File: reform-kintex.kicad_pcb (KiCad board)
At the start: 8 copper layers, 60 x 67.8 mm, 38 parts, among them J1 Conn_01x33, U1 MNT Reform 2.0 SoM Socket, U2 XC7K160T-FFG676, U3 MT41K512M16HA-125 :A, U4 MT41K512M16HA-125 :A, U5 TPS51200DRC, U6 KSZ9031RNXCA, U7 TUSB1310ZAY, U8 TC358867XBG, U9 SiI9022A

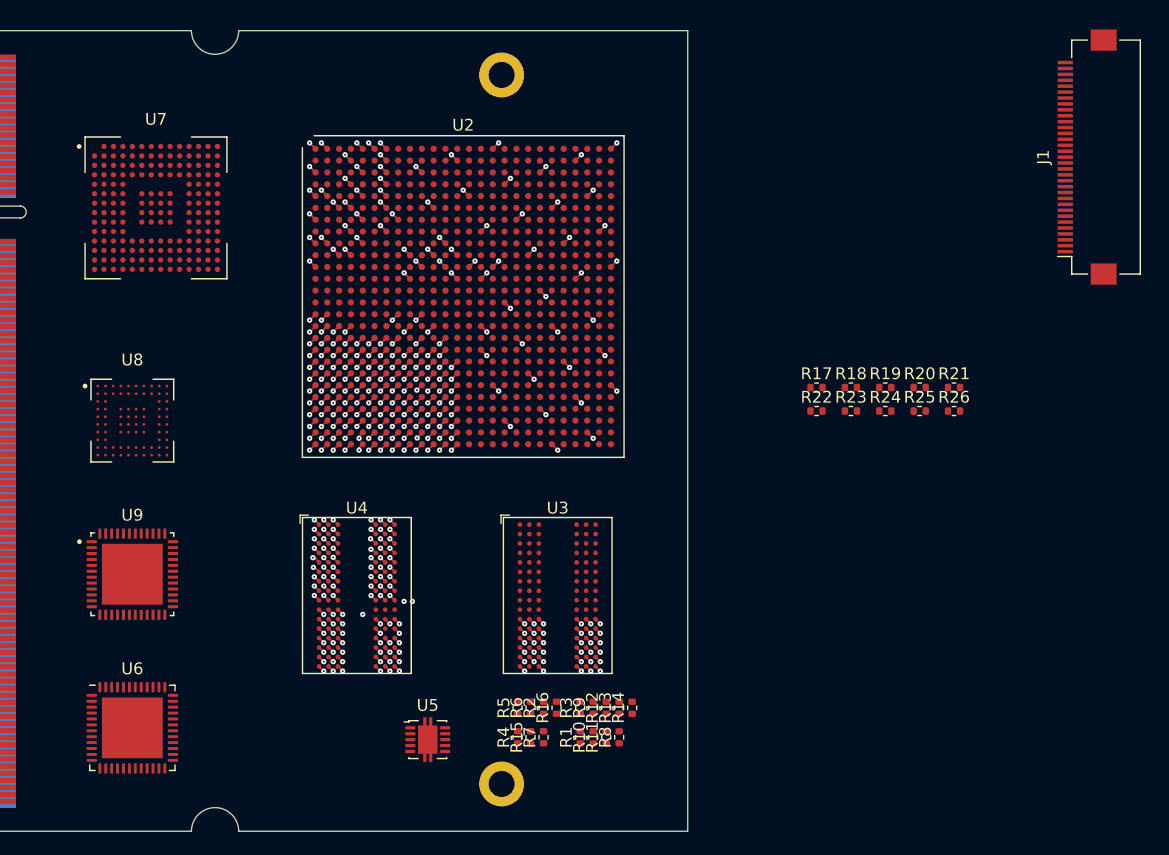
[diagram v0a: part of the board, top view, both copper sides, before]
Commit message: some work on 6 power supplies, SPI flash
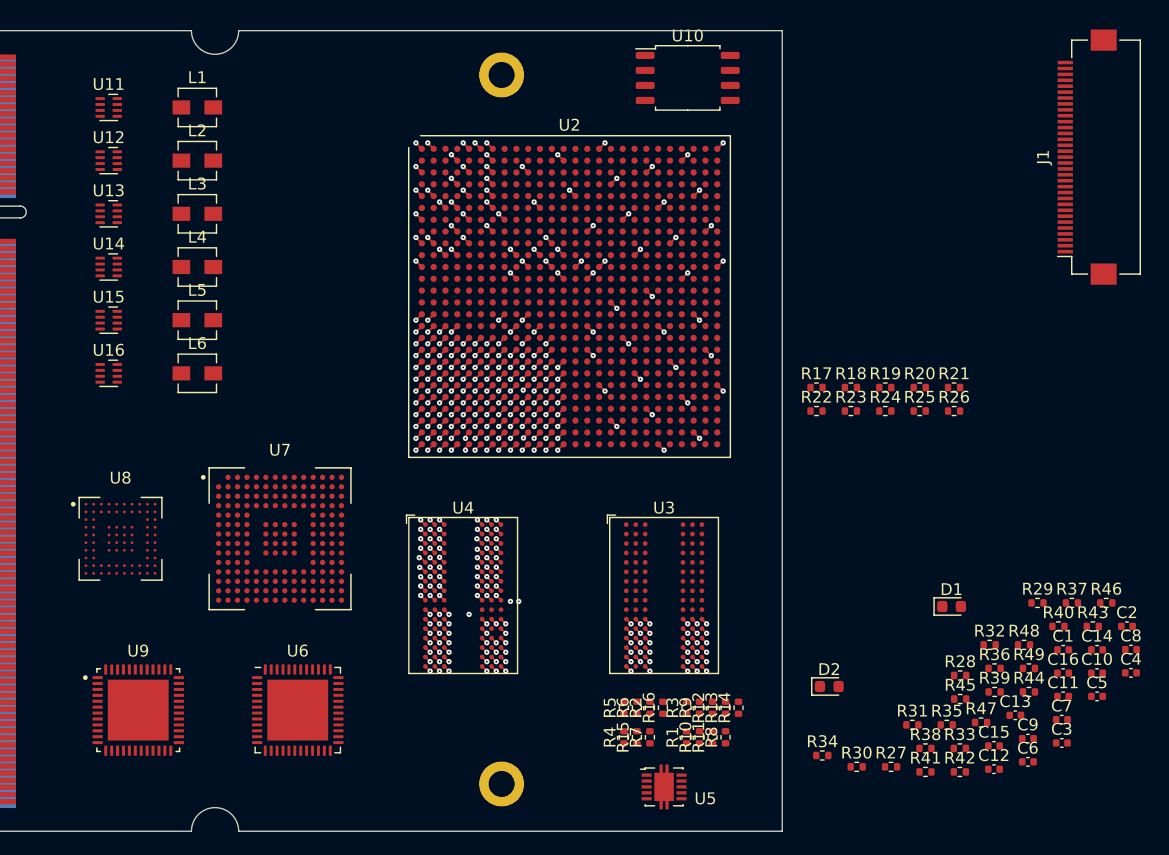
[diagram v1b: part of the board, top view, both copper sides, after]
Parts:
- added C1: 0.1uF, Capacitor_SMD:C_0402_1005Metric, F.Cu at (191.8, 152.4)
- added C10: 0.1uF, Capacitor_SMD:C_0402_1005Metric, F.Cu at (194.6, 154.4)
- added C11: 120p, Capacitor_SMD:C_0402_1005Metric, F.Cu at (191.8, 156.3)
- added C12: 120p, Capacitor_SMD:C_0402_1005Metric, F.Cu at (185.9, 162.5)
- added C13: 120p, Capacitor_SMD:C_0402_1005Metric, F.Cu at (187.7, 157.9)
- added C14: 120p, Capacitor_SMD:C_0402_1005Metric, F.Cu at (194.6, 152.4)
- added C15: 120p, Capacitor_SMD:C_0402_1005Metric, F.Cu at (185.9, 160.5)
- added C16: 120p, Capacitor_SMD:C_0402_1005Metric, F.Cu at (191.8, 154.4)
- added C2: 0.1uF, Capacitor_SMD:C_0402_1005Metric, F.Cu at (197.2, 150.4)
- added C3: 0.1uF, Capacitor_SMD:C_0402_1005Metric, F.Cu at (191.7, 160.3)
- added C4: 0.1uF, Capacitor_SMD:C_0402_1005Metric, F.Cu at (197.5, 154.3)
- added C5: 0.1uF, Capacitor_SMD:C_0402_1005Metric, F.Cu at (194.6, 156.3)
- added C6: 0.1uF, Capacitor_SMD:C_0402_1005Metric, F.Cu at (188.8, 161.9)
- added C7: 0.1uF, Capacitor_SMD:C_0402_1005Metric, F.Cu at (191.7, 158.3)
- added C8: 0.1uF, Capacitor_SMD:C_0402_1005Metric, F.Cu at (197.5, 152.4)
- added C9: 0.1uF, Capacitor_SMD:C_0402_1005Metric, F.Cu at (188.8, 159.9)
- added D1: LED_Small, LED_SMD:LED_0603_1608Metric, F.Cu at (182.3, 148.7)
- added D2: LED_Small, LED_SMD:LED_0603_1608Metric, F.Cu at (172.0, 155.5)
- added L1: IHLP1212AEERR47M11, Inductor_SMD:L_Vishay_IHLP-1212, F.Cu at (118.5, 106.5)
- added L2: IHLP1212AEERR47M11, Inductor_SMD:L_Vishay_IHLP-1212, F.Cu at (118.5, 111.0)
- added L3: IHLP1212AEERR47M11, Inductor_SMD:L_Vishay_IHLP-1212, F.Cu at (118.5, 115.5)
- added L4: IHLP1212AEERR47M11, Inductor_SMD:L_Vishay_IHLP-1212, F.Cu at (118.5, 120.0)
- added L5: IHLP1212AEERR47M11, Inductor_SMD:L_Vishay_IHLP-1212, F.Cu at (118.5, 124.5)
- added L6: IHLP1212AEERR47M11, Inductor_SMD:L_Vishay_IHLP-1212, F.Cu at (118.5, 129.0)
- added R27: 2k2, Resistor_SMD:R_0402_1005Metric, F.Cu at (177.2, 162.3)
- added R28: 0, Resistor_SMD:R_0402_1005Metric, F.Cu at (183.1, 154.6)
- added R29: 0, Resistor_SMD:R_0402_1005Metric, F.Cu at (189.6, 148.4)
- added R30: 4k7, Resistor_SMD:R_0402_1005Metric, F.Cu at (174.3, 162.3)
- added R31: 4k7, Resistor_SMD:R_0402_1005Metric, F.Cu at (179.0, 158.8)
- added R32: R_Small, Resistor_SMD:R_0402_1005Metric, F.Cu at (185.6, 152.0)
- added R33: 453k, Resistor_SMD:R_0402_1005Metric, F.Cu at (183.0, 160.7)
- added R34: 100k_1%, Resistor_SMD:R_0402_1005Metric, F.Cu at (171.4, 161.3)
- added R35: R_Small, Resistor_SMD:R_0402_1005Metric, F.Cu at (181.9, 158.8)
- added R36: 66.5k, Resistor_SMD:R_0402_1005Metric, F.Cu at (186.0, 154.0)
- added R37: 100k_1%, Resistor_SMD:R_0402_1005Metric, F.Cu at (192.5, 148.4)
- added R38: R_Small, Resistor_SMD:R_0402_1005Metric, F.Cu at (180.1, 160.7)
- added R39: 200k, Resistor_SMD:R_0402_1005Metric, F.Cu at (186.0, 156.0)
- added R40: 100k_1%, Resistor_SMD:R_0402_1005Metric, F.Cu at (191.4, 150.4)
- added R41: R_Small, Resistor_SMD:R_0402_1005Metric, F.Cu at (180.1, 162.7)
- added R42: 150k, Resistor_SMD:R_0402_1005Metric, F.Cu at (183.0, 162.7)
- added R43: 100k_1%, Resistor_SMD:R_0402_1005Metric, F.Cu at (194.3, 150.4)
- added R44: R_Small, Resistor_SMD:R_0402_1005Metric, F.Cu at (188.9, 156.0)
- added R45: 83.5k, Resistor_SMD:R_0402_1005Metric, F.Cu at (183.1, 156.6)
- added R46: 100k_1%, Resistor_SMD:R_0402_1005Metric, F.Cu at (195.4, 148.4)
- added R47: R_Small, Resistor_SMD:R_0402_1005Metric, F.Cu at (184.8, 158.6)
- added R48: 100k, Resistor_SMD:R_0402_1005Metric, F.Cu at (188.5, 152.0)
- added R49: 100k_1%, Resistor_SMD:R_0402_1005Metric, F.Cu at (188.9, 154.0)
- added U10: W25Q128JVS, Package_SO:SOIC-8_5.23x5.23mm_P1.27mm, F.Cu at (160.0, 104.0)
- added U11: TPS62823DLC, Package_DFN_QFN:Texas_VSON-HR-8_1.5x2mm_P0.5mm, F.Cu at (111.0, 106.5)
- added U12: TPS62823DLC, Package_DFN_QFN:Texas_VSON-HR-8_1.5x2mm_P0.5mm, F.Cu at (111.0, 111.0)
- added U13: TPS62823DLC, Package_DFN_QFN:Texas_VSON-HR-8_1.5x2mm_P0.5mm, F.Cu at (111.0, 115.5)
- added U14: TPS62823DLC, Package_DFN_QFN:Texas_VSON-HR-8_1.5x2mm_P0.5mm, F.Cu at (111.0, 120.0)
- added U15: TPS62823DLC, Package_DFN_QFN:Texas_VSON-HR-8_1.5x2mm_P0.5mm, F.Cu at (111.0, 124.5)
- added U16: TPS62823DLC, Package_DFN_QFN:Texas_VSON-HR-8_1.5x2mm_P0.5mm, F.Cu at (111.0, 129.0)
- moved U7 29.9 mm to (125.5, 143.0)
- moved U5 20.4 mm to (158.0, 164.0)
- moved U6 14.1 mm to (127.0, 157.5)
- moved U9 11.5 mm to (113.5, 157.5)
- moved U8 10.0 mm to (112.0, 143.0)
- moved R1 9.00 mm to (159.9, 159.8)
- moved R10 9.00 mm to (161.0, 159.8)
- moved R11 9.00 mm to (162.1, 159.8)
- moved R12 9.00 mm to (162.1, 157.3)
- moved R13 9.00 mm to (163.2, 157.3)
- moved R14 9.00 mm to (164.3, 157.3)
- moved R15 9.00 mm to (155.7, 159.8)
- moved R16 9.00 mm to (157.9, 157.3)
- moved R2 9.00 mm to (156.8, 157.3)
- moved R3 9.00 mm to (159.9, 157.3)
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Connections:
- R22 pad 2: Net-(R22-Pad2) -> SOC_RESETn
- U2 pad A21: Net-(U2-PadA21) -> +3V3
- U2 pad A22: Net-(U2-PadA22) -> QSPI_DQ3
- U2 pad A25: Net-(U2-PadA25) -> QSPI_DQ1
- U2 pad B18: Net-(U2-PadB18) -> +3V3
- U2 pad B22: Net-(U2-PadB22) -> QSPI_DQ2
- U2 pad B24: Net-(U2-PadB24) -> QSPI_DQ0
- U2 pad C25: Net-(U2-PadC25) -> +3V3
- U2 pad D22: Net-(U2-PadD22) -> +3V3
- U2 pad E19: Net-(U2-PadE19) -> +3V3
- U2 pad E8: Net-(U2-PadE8) -> +1V8
- U2 pad F16: Net-(U2-PadF16) -> +3V3
- U2 pad F26: Net-(U2-PadF26) -> +3V3
- U2 pad G23: Net-(U2-PadG23) -> +3V3
- U2 pad H20: Net-(U2-PadH20) -> +3V3
- U2 pad J17: Net-(U2-PadJ17) -> +3V3
- U2 pad L21: Net-(U2-PadL21) -> +3V3
- U2 pad M12: Net-(U2-PadM12) -> +1V8
- U2 pad M18: Net-(U2-PadM18) -> +3V3
- U2 pad P6: Net-(R22-Pad2) -> SOC_RESETn
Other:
- board size 60 x 67.8 mm -> 68 x 67.8 mm

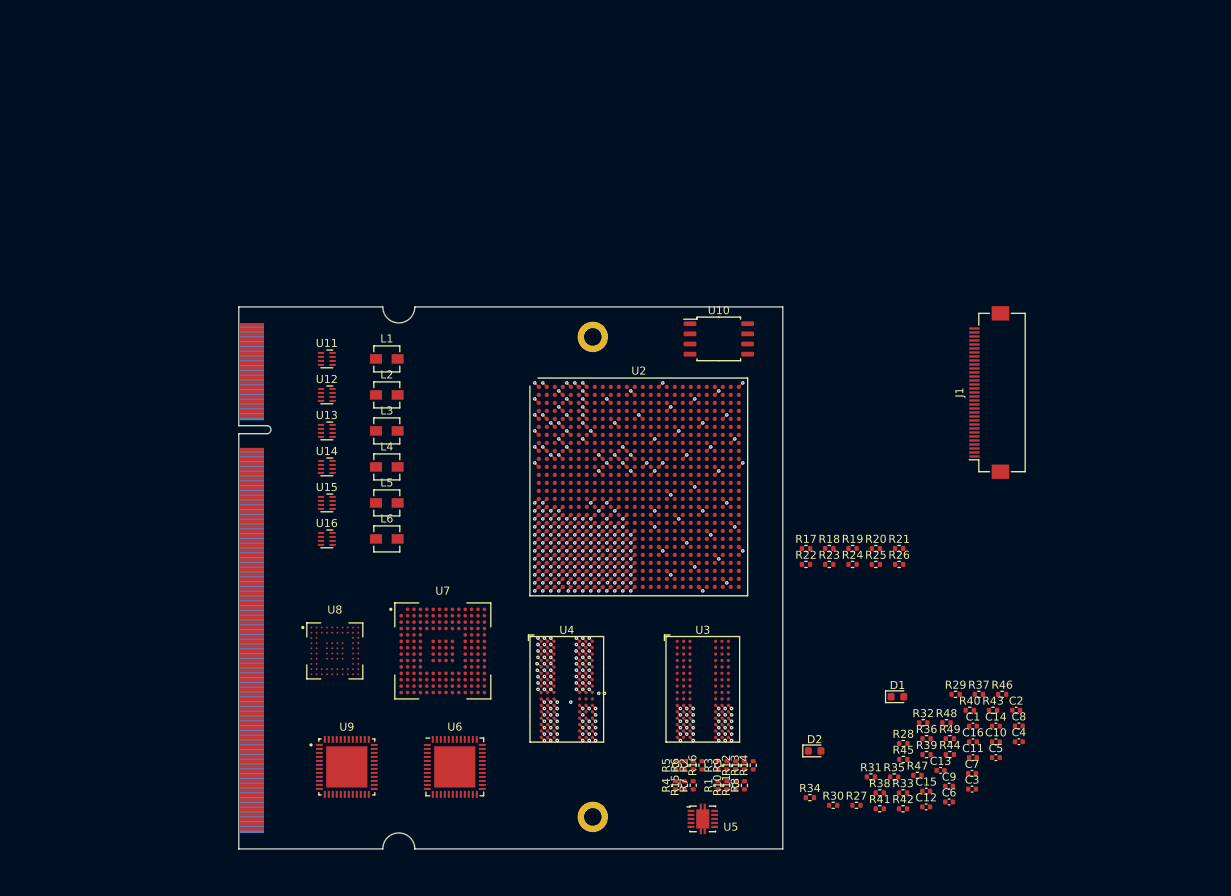
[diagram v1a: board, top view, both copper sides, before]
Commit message: more DDR3 routing
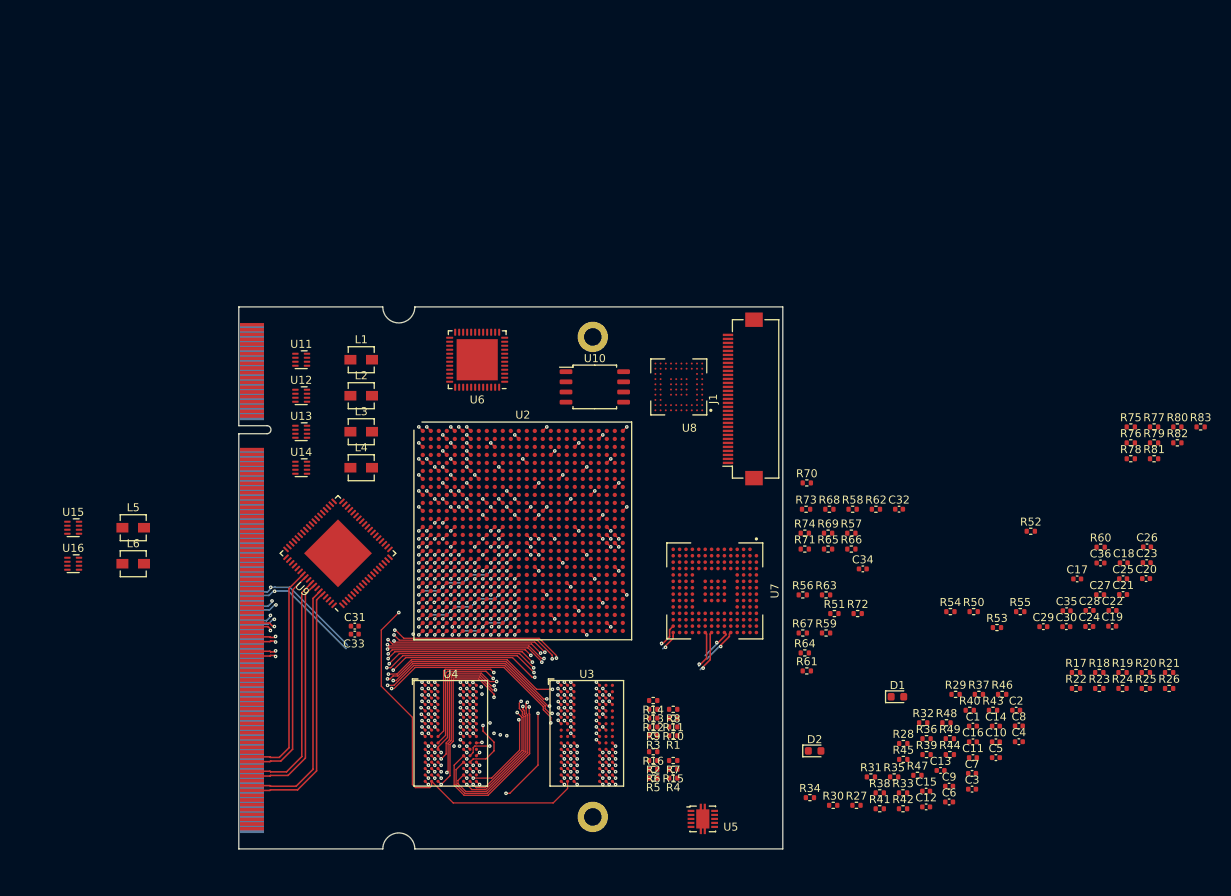
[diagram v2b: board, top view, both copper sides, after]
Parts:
- added C17: 10uF, Capacitor_SMD:C_0402_1005Metric, F.Cu at (204.8, 134.0)
- added C18: 10uF, Capacitor_SMD:C_0402_1005Metric, F.Cu at (210.6, 132.0)
- added C19: 10uF, Capacitor_SMD:C_0402_1005Metric, F.Cu at (209.2, 139.9)
- added C20: 10uF, Capacitor_SMD:C_0402_1005Metric, F.Cu at (213.4, 134.0)
- added C21: 10uF, Capacitor_SMD:C_0402_1005Metric, F.Cu at (210.5, 135.9)
- added C22: 1nF, Capacitor_SMD:C_0402_1005Metric, F.Cu at (209.2, 137.9)
- added C23: 0.1uF, Capacitor_SMD:C_0402_1005Metric, F.Cu at (213.5, 132.0)
- added C24: 10nF, Capacitor_SMD:C_0402_1005Metric, F.Cu at (206.3, 139.9)
- added C25: 10nF, Capacitor_SMD:C_0402_1005Metric, F.Cu at (210.5, 134.0)
- added C26: 10nF, Capacitor_SMD:C_0402_1005Metric, F.Cu at (213.5, 130.0)
- added C27: 10nF, Capacitor_SMD:C_0402_1005Metric, F.Cu at (207.7, 136.0)
- added C28: 0.1uF, Capacitor_SMD:C_0402_1005Metric, F.Cu at (206.3, 137.9)
- added C29: 22pF, Capacitor_SMD:C_0402_1005Metric, F.Cu at (200.6, 140.0)
- added C30: 22pF, Capacitor_SMD:C_0402_1005Metric, F.Cu at (203.4, 140.0)
- added C31: 0.1uF, Capacitor_SMD:C_0402_1005Metric, F.Cu at (114.5, 139.9)
- added C32: 4.7nF, Capacitor_SMD:C_0402_1005Metric, F.Cu at (182.5, 125.3)
- added C33: 0.1uF, Capacitor_SMD:C_0402_1005Metric, F.Cu at (114.5, 140.9)
- added C34: 4.7nF, Capacitor_SMD:C_0402_1005Metric, F.Cu at (178.0, 132.8)
- added C35: 22pF, Capacitor_SMD:C_0402_1005Metric, F.Cu at (203.5, 138.0)
- added C36: 22pF, Capacitor_SMD:C_0402_1005Metric, F.Cu at (207.7, 132.0)
- added R50: 10k, Resistor_SMD:R_0402_1005Metric, F.Cu at (191.9, 138.1)
- added R51: 10k, Resistor_SMD:R_0402_1005Metric, F.Cu at (174.4, 138.3)
- added R52: 10k, Resistor_SMD:R_0402_1005Metric, F.Cu at (199.0, 128.0)
- added R53: 10k, Resistor_SMD:R_0402_1005Metric, F.Cu at (194.8, 140.1)
- added R54: 1.8M, Resistor_SMD:R_0402_1005Metric, F.Cu at (188.9, 138.1)
- added R55: 12.1k, Resistor_SMD:R_0402_1005Metric, F.Cu at (197.7, 138.1)
- added R56: 10k, Resistor_SMD:R_0402_1005Metric, F.Cu at (170.5, 136.0)
- added R57: 10k, Resistor_SMD:R_0402_1005Metric, F.Cu at (176.6, 128.3)
- added R58: 90.9k 1%, Resistor_SMD:R_0402_1005Metric, F.Cu at (176.7, 125.3)
- added R59: 10k 1%, Resistor_SMD:R_0402_1005Metric, F.Cu at (173.4, 140.8)
- added R60: 10k 1%, Resistor_SMD:R_0402_1005Metric, F.Cu at (207.7, 130.0)
- added R61: DNP, Resistor_SMD:R_0402_1005Metric, F.Cu at (171.0, 145.5)
- added R62: DNP, Resistor_SMD:R_0402_1005Metric, F.Cu at (179.6, 125.3)
- added R63: DNP, Resistor_SMD:R_0402_1005Metric, F.Cu at (173.4, 136.0)
- added R64: DNP, Resistor_SMD:R_0402_1005Metric, F.Cu at (170.8, 143.2)
- added R65: 1.8M, Resistor_SMD:R_0402_1005Metric, F.Cu at (173.7, 130.3)
- added R66: DNP, Resistor_SMD:R_0402_1005Metric, F.Cu at (176.6, 130.3)
- added R67: DNP, Resistor_SMD:R_0402_1005Metric, F.Cu at (170.5, 140.8)
- added R68: DNP, Resistor_SMD:R_0402_1005Metric, F.Cu at (173.8, 125.3)
- added R69: DNP, Resistor_SMD:R_0402_1005Metric, F.Cu at (173.7, 128.3)
- added R70: DNP, Resistor_SMD:R_0402_1005Metric, F.Cu at (171.0, 122.0)
- added R71: 0, Resistor_SMD:R_0402_1005Metric, F.Cu at (170.8, 130.3)
- added R72: DNP, Resistor_SMD:R_0402_1005Metric, F.Cu at (177.4, 138.3)
- added R73: DNP, Resistor_SMD:R_0402_1005Metric, F.Cu at (170.9, 125.3)
- added R74: DNP, Resistor_SMD:R_0402_1005Metric, F.Cu at (170.8, 128.3)
- added R75: 4.7k, Resistor_SMD:R_0402_1005Metric, F.Cu at (211.5, 115.0)
- added R76: 330, Resistor_SMD:R_0402_1005Metric, F.Cu at (211.5, 117.0)
- added R77: 100, Resistor_SMD:R_0402_1005Metric, F.Cu at (214.4, 115.0)
- added R78: DNP, Resistor_SMD:R_0402_1005Metric, F.Cu at (211.5, 119.0)
- added R79: 0, Resistor_SMD:R_0402_1005Metric, F.Cu at (214.4, 117.0)
- added R80: 0, Resistor_SMD:R_0402_1005Metric, F.Cu at (217.3, 115.0)
- added R81: 0, Resistor_SMD:R_0402_1005Metric, F.Cu at (214.4, 119.0)
- added R82: DNP, Resistor_SMD:R_0402_1005Metric, F.Cu at (217.3, 117.0)
- added R83: DNP, Resistor_SMD:R_0402_1005Metric, F.Cu at (220.2, 115.0)
- R23: value 4.7k -> ???
- U3, U4: value MT41K512M16HA-125 :A -> IS43TR16512B-125KBLI
- U8: value TC358867XBG -> TC358778XBG
- U9: footprint footprints:QFN50P700X700X100-49N -> Package_DFN_QFN:QFN-72-1EP_10x10mm_P0.5mm_EP6x6mm
- moved U8 54.2 mm to (155.0, 110.0), turned to 180 degrees
- moved U6 51.0 mm to (129.8, 106.6), turned to 180 degrees
- moved R17 37.1 mm to (204.7, 145.7)
- moved R18 37.1 mm to (207.6, 145.7)
- moved R19 37.1 mm to (210.5, 145.7)
- moved R20 37.1 mm to (213.4, 145.7)
- moved R21 37.1 mm to (216.3, 145.7)
- moved R22 37.1 mm to (204.7, 147.7)
- moved R23 37.1 mm to (207.6, 147.7)
- moved R24 37.1 mm to (210.5, 147.7)
- moved R25 37.1 mm to (213.4, 147.7)
- moved R26 37.1 mm to (216.3, 147.7)
- moved U7 34.8 mm to (159.5, 135.5), turned to 270 degrees
- moved L5 31.9 mm to (86.8, 127.6)
- moved L6 31.9 mm to (86.8, 132.1)
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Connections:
- net DPLP1- renamed Net-(U8-PadK6)
- net Net-(U2-PadP5) renamed MODE2
- net Net-(U8-PadA8) renamed I2C1_SCL
- C1 pad 2: Vtt -> VTTREF
- C2 pad 2: Vtt -> VTTREF
- C3 pad 2: Vtt -> VTTREF
- U2 pad A11: Net-(U2-PadA11) -> +1V8
- U2 pad A8: Net-(U2-PadA8) -> DISP1_RGB6
- U2 pad A9: Net-(U2-PadA9) -> DISP1_RGB7
- U2 pad AA14: Net-(U2-PadAA14) -> DISP2_RGB11
- U2 pad AA15: Net-(U2-PadAA15) -> DISP2_RGB10
- U2 pad AA17: Net-(U2-PadAA17) -> DISP2_RGB3
- U2 pad AA18: Net-(U2-PadAA18) -> DISP2_RGB2
- U2 pad AA21: Net-(U2-PadAA21) -> +1V8
- U2 pad AA3: RAM_D15 -> RAM_D10
- U2 pad AB11: Net-(U2-PadAB11) -> RAM_A8
- U2 pad AB14: Net-(U2-PadAB14) -> DISP2_RGB5
- U2 pad AB15: Net-(U2-PadAB15) -> DISP2_RGB4
- U2 pad AB16: Net-(U2-PadAB16) -> DISP2_RGB1
- U2 pad AB17: Net-(U2-PadAB17) -> DISP2_HS
- U2 pad AB18: Net-(U2-PadAB18) -> +1V8
- U2 pad AB2: RAM_D13 -> RAM_D14
- U2 pad AB21: Net-(U2-PadAB21) -> TUSB_PDOWN1
- U2 pad AB22: Net-(U2-PadAB22) -> TUSB_TX_DETRX_LPBK
- U2 pad AB9: RAM_CAS# -> RAM_BA2
- U2 pad AC11: Net-(U2-PadAC11) -> RAM_A5
- U2 pad AC14: Net-(U2-PadAC14) -> DISP2_RGB9
- U2 pad AC15: Net-(U2-PadAC15) -> +1V8
- U2 pad AC16: Net-(U2-PadAC16) -> DISP2_RGB0
- U2 pad AC17: Net-(U2-PadAC17) -> DISP2_VS
- U2 pad AC18: Net-(U2-PadAC18) -> DISP2_PCLK
- U2 pad AC2: RAM_D14 -> RAM_D12
- U2 pad AC21: Net-(U2-PadAC21) -> TUSB_TX_ELECIDLE
- U2 pad AC22: Net-(U2-PadAC22) -> TUSB_PDOWN0
- U2 pad AC25: Net-(U2-PadAC25) -> +1V8
- U2 pad AD14: Net-(U2-PadAD14) -> DISP2_RGB8
- U2 pad AD15: Net-(U2-PadAD15) -> DISP2_RGB17
- U2 pad AD16: Net-(U2-PadAD16) -> DISP2_RGB13
- U2 pad AD20: Net-(U2-PadAD20) -> DISP2_DE
- U2 pad AD21: Net-(U2-PadAD21) -> TUSB_RX_ELECIDLE
- U2 pad AD22: Net-(U2-PadAD22) -> +1V8
- U2 pad AD23: Net-(U2-PadAD23) -> TUSB_PWRPRESENT
- U2 pad AD24: Net-(U2-PadAD24) -> TUSB_PHYRESETN
- U2 pad AD25: Net-(U2-PadAD25) -> TUSB_ULPI_D3
- U2 pad AD26: Net-(U2-PadAD26) -> TUSB_ULPI_STP
- U2 pad AD3: Vtt -> VTTREF
- U2 pad AD5: Net-(U2-PadAD5) -> RAM_DM1
- U2 pad AD8: RAM_BA2 -> RAM_CAS#
- U2 pad AE11: Vtt -> VTTREF
- U2 pad AE15: Net-(U2-PadAE15) -> DISP2_RGB16
- U2 pad AE16: Net-(U2-PadAE16) -> DISP2_RGB12
- U2 pad AE17: Net-(U2-PadAE17) -> DISP2_RGB23
- U2 pad AE18: Net-(U2-PadAE18) -> DISP2_RGB19
- U2 pad AE19: Net-(U2-PadAE19) -> +1V8
- U2 pad AE21: Net-(U2-PadAE21) -> TUSB_PHY_STATUS
- U2 pad AE22: Net-(U2-PadAE22) -> TUSB_ULPI_D5
- U2 pad AE23: Net-(U2-PadAE23) -> TUSB_ULPI_D1
- U2 pad AE25: Net-(U2-PadAE25) -> TUSB_ULPI_D4
- U2 pad AE26: Net-(U2-PadAE26) -> TUSB_ULPI_D0
- U2 pad AF14: Net-(U2-PadAF14) -> DISP2_RGB21
- U2 pad AF15: Net-(U2-PadAF15) -> DISP2_RGB20
- U2 pad AF16: Net-(U2-PadAF16) -> +1V8
- U2 pad AF17: Net-(U2-PadAF17) -> DISP2_RGB22
- U2 pad AF18: Net-(U2-PadAF18) -> DISP2_RGB18
- U2 pad AF19: Net-(U2-PadAF19) -> DISP2_RGB15
- U2 pad AF20: Net-(U2-PadAF20) -> DISP2_RGB14
- U2 pad AF22: Net-(U2-PadAF22) -> TUSB_ULPI_D6
- U2 pad AF23: Net-(U2-PadAF23) -> TUSB_ULPI_D2
- U2 pad AF24: Net-(U2-PadAF24) -> TUSB_ULPI_DIR
- U2 pad AF25: Net-(U2-PadAF25) -> TUSB_ULPI_NXT
- U2 pad AF26: Net-(U2-PadAF26) -> +1V8
- U2 pad B25: Net-(U2-PadB25) -> PUDC_B
- U2 pad B8: Net-(U2-PadB8) -> +1V8
- U2 pad B9: Net-(U2-PadB9) -> DISP1_RGB4
- U2 pad C12: Net-(U2-PadC12) -> DISP1_CLK
- U2 pad C15: Net-(U2-PadC15) -> +1V8
- U2 pad C23: Net-(U2-PadC23) -> FCS_B
- U2 pad C8: Net-(U2-PadC8) -> CCLK
- U2 pad C9: Net-(U2-PadC9) -> DISP1_RGB5
- U2 pad D10: Net-(U2-PadD10) -> DISP1_RGB0
- U2 pad D11: Net-(U2-PadD11) -> DISP1_VS
- U2 pad D12: Net-(U2-PadD12) -> +1V8
- U2 pad D18: Net-(U2-PadD18) -> ETH_TX_CLK
- U2 pad D19: Net-(U2-PadD19) -> ETH_RX_D1
- U2 pad D20: Net-(U2-PadD20) -> ETH_RX_D2
- U2 pad D8: Net-(U2-PadD8) -> DISP1_RGB8
- U2 pad D9: Net-(U2-PadD9) -> DISP1_RGB9
- U2 pad E10: Net-(U2-PadE10) -> DISP1_RGB1
- U2 pad E11: Net-(U2-PadE11) -> DISP1_HS
- U2 pad E15: Net-(U2-PadE15) -> ETH_INT_N
- U2 pad E16: Net-(U2-PadE16) -> ETH_RST_N
- U2 pad E17: Net-(U2-PadE17) -> ETH_TX_D2
- U2 pad E18: Net-(U2-PadE18) -> ETH_TX_D3
- U2 pad E9: Net-(U2-PadE9) -> +1V8
- U2 pad F10: Net-(U2-PadF10) -> DISP1_RGB2
- U2 pad F14: Net-(U2-PadF14) -> DISP1_DE
- U2 pad F15: Net-(U2-PadF15) -> ETH_REF_CLK
- U2 pad F17: Net-(U2-PadF17) -> ETH_TX_D1
- U2 pad F18: Net-(U2-PadF18) -> ETH_TX_D0
- U2 pad F20: Net-(U2-PadF20) -> ETH_RX_CLK
- U2 pad F8: Net-(U2-PadF8) -> DISP1_RGB10
- U2 pad F9: Net-(U2-PadF9) -> DISP1_RGB11
- U2 pad G10: Net-(U2-PadG10) -> DISP1_RGB21
- U2 pad G11: Net-(U2-PadG11) -> DISP1_RGB3
- U2 pad G13: Net-(U2-PadG13) -> +1V8
- U2 pad G14: Net-(U2-PadG14) -> DISP1_RGB14
- U2 pad G17: Net-(U2-PadG17) -> ETH_TX_EN
- U2 pad G19: Net-(U2-PadG19) -> ETH_RX_D3
- U2 pad G9: Net-(U2-PadG9) -> DISP1_RGB20
- U2 pad H10: Net-(U2-PadH10) -> +1V8
- U2 pad H11: Net-(U2-PadH11) -> DISP1_RGB12
- U2 pad H12: Net-(U2-PadH12) -> DISP1_RGB13
- U2 pad H13: Net-(U2-PadH13) -> DISP1_RGB18
- U2 pad H14: Net-(U2-PadH14) -> DISP1_RGB15
- U2 pad H17: Net-(U2-PadH17) -> ETH_RX_DV
- U2 pad H18: Net-(U2-PadH18) -> ETH_RX_D0
- U2 pad H8: Net-(U2-PadH8) -> DISP1_RGB22
- U2 pad H9: Net-(U2-PadH9) -> DISP1_RGB23
- U2 pad J10: Net-(U2-PadJ10) -> DISP1_RGB16
- U2 pad J11: Net-(U2-PadJ11) -> DISP1_RGB17
- U2 pad J13: Net-(U2-PadJ13) -> DISP1_RGB19
- U2 pad J15: Net-(U2-PadJ15) -> ETH_MDIO
- U2 pad J16: Net-(U2-PadJ16) -> ETH_MDC
- U2 pad K24: Net-(U2-PadK24) -> +1V8
- U2 pad K25: Net-(U2-PadK25) -> TUSB_RX_STAT2
- U2 pad K26: Net-(U2-PadK26) -> TUSB_RX_STAT1
- U2 pad L24: Net-(U2-PadL24) -> TUSB_RX_D11
- U2 pad L25: Net-(U2-PadL25) -> TUSB_RX_D1
- U2 pad M19: Net-(U2-PadM19) -> TUSB_TX_D13
- U2 pad M20: Net-(U2-PadM20) -> TUSB_RX_D9
- U2 pad M21: Net-(U2-PadM21) -> TUSB_RX_D14
- U2 pad M22: Net-(U2-PadM22) -> TUSB_RX_D15
- U2 pad M24: Net-(U2-PadM24) -> TUSB_RX_D10
- U2 pad M25: Net-(U2-PadM25) -> TUSB_RX_D0
- U2 pad M26: Net-(U2-PadM26) -> TUSB_RX_D5
- U2 pad N12: Net-(U2-PadN12) -> GND
- U2 pad N17: Net-(U2-PadN17) -> TUSB_TX_D9
- U2 pad N18: Net-(U2-PadN18) -> TUSB_TX_D12
- U2 pad N19: Net-(U2-PadN19) -> TUSB_RX_D8
- U2 pad N21: Net-(U2-PadN21) -> TUSB_TXCLK
- U2 pad N23: Net-(U2-PadN23) -> TUSB_RX_K0
- U2 pad N24: Net-(U2-PadN24) -> TUSB_RX_D3
- U2 pad N25: Net-(U2-PadN25) -> +1V8
- U2 pad N26: Net-(U2-PadN26) -> TUSB_RX_D4
- U2 pad P11: Net-(U2-PadP11) -> GND
- U2 pad P16: Net-(U2-PadP16) -> TUSB_TX_D8
- U2 pad P18: Net-(U2-PadP18) -> TUSB_TX_DATAK0
- U2 pad P19: Net-(U2-PadP19) -> TUSB_RX_D12
- U2 pad P20: Net-(U2-PadP20) -> TUSB_RX_D13
- U2 pad P22: Net-(U2-PadP22) -> +1V8
- U2 pad P23: Net-(U2-PadP23) -> TUSB_RX_K1
- U2 pad P24: Net-(U2-PadP24) -> TUSB_RX_D2
- U2 pad P25: Net-(U2-PadP25) -> TUSB_RX_D7
- U2 pad P26: Net-(U2-PadP26) -> TUSB_RX_VALID
- U2 pad R11: Net-(U2-PadR11) -> GND
- U2 pad R12: Net-(U2-PadR12) -> GND
- U2 pad R16: Net-(U2-PadR16) -> TUSB_TX_D10
- U2 pad R17: Net-(U2-PadR17) -> TUSB_TX_D11
- U2 pad R18: Net-(U2-PadR18) -> TUSB_TX_DATAK1
- U2 pad R19: Net-(U2-PadR19) -> +1V8
- U2 pad R20: Net-(U2-PadR20) -> TUSB_TX_D1
- U2 pad R21: Net-(U2-PadR21) -> TUSB_PCLK
- U2 pad R25: Net-(U2-PadR25) -> TUSB_RX_D6
- U2 pad R26: Net-(U2-PadR26) -> TUSB_RX_STAT0
- U2 pad T16: Net-(U2-PadT16) -> +1V8
- U2 pad T17: Net-(U2-PadT17) -> TUSB_TX_D15
- U2 pad T18: Net-(U2-PadT18) -> TUSB_TX_D6
- U2 pad T19: Net-(U2-PadT19) -> TUSB_TX_D7
- U2 pad T2: Net-(U2-PadT2) -> MODE1
- U2 pad T20: Net-(U2-PadT20) -> TUSB_TX_D0
- U2 pad T22: Net-(U2-PadT22) -> TUSB_TX_D2
- U2 pad T23: Net-(U2-PadT23) -> TUSB_TX_D3
- U2 pad T26: Net-(U2-PadT26) -> +1V8
- U2 pad T5: Net-(U2-PadT5) -> MODE0
- U2 pad U1: RAM_D2 -> RAM_D9
- U2 pad U17: Net-(U2-PadU17) -> TUSB_TX_D14
- U2 pad U19: Net-(U2-PadU19) -> TUSB_TX_D4
- U2 pad U2: RAM_D1 -> RAM_D13
- U2 pad U20: Net-(U2-PadU20) -> TUSB_TX_D5
- U2 pad U23: Net-(U2-PadU23) -> +1V8
- U2 pad U5: RAM_D0 -> RAM_D2
- U2 pad U7: RAM_D5 -> RAM_D4
- U2 pad V1: RAM_D10 -> RAM_D15
- U2 pad V11: RAM_A14 -> RAM_A11
- U2 pad V2: RAM_D9 -> RAM_D7
- U2 pad V20: Net-(U2-PadV20) -> +1V8
- U2 pad V3: RAM_D3 -> RAM_D11
- U2 pad V4: RAM_D7 -> RAM_D0
- U2 pad V7: RAM_A11 -> RAM_A15
- U2 pad W1: RAM_D11 -> RAM_D5
- U2 pad W17: Net-(U2-PadW17) -> +1V8
- U2 pad W20: Net-(U2-PadW20) -> TUSB_ENAB
- U2 pad W3: RAM_D4 -> RAM_D1
- U2 pad W4: Vtt -> VTTREF
- U2 pad W8: RAM_A5 -> VTTREF
- U2 pad Y1: RAM_D12 -> RAM_D3
- U2 pad Y11: RAM_A8 -> RAM_A14
- U2 pad Y14: Net-(U2-PadY14) -> +1V8
- U2 pad Y15: Net-(U2-PadY15) -> DISP2_RGB7
- U2 pad Y16: Net-(U2-PadY16) -> DISP2_RGB6
- U2 pad Y20: Net-(U2-PadY20) -> TUSB_ULPI_D7
- U2 pad Y21: Net-(U2-PadY21) -> TUSB_RESETN
- U2 pad Y22: Net-(U2-PadY22) -> TUSB_ULPI_CLK
- U2 pad Y24: Net-(U2-PadY24) -> +1V8
- U2 pad Y3: RAM_DM1 -> Net-(U2-PadY3)
- U3 pad A1: Net-(U3-PadA1) -> +1V5
- U3 pad A8: Net-(U3-PadA1) -> +1V5
- U3 pad B2: Net-(U3-PadB2) -> +1V5
- U3 pad C1: Net-(U3-PadA1) -> +1V5
- U3 pad C9: Net-(U3-PadA1) -> +1V5
- U3 pad D2: Net-(U3-PadA1) -> +1V5
- U3 pad D9: Net-(U3-PadB2) -> +1V5
- U3 pad E9: Net-(U3-PadA1) -> +1V5
- U3 pad F1: Net-(U3-PadA1) -> +1V5
- U3 pad G7: Net-(U3-PadB2) -> +1V5
- U3 pad H1: Net-(U3-PadH1) -> VTTREF
- U3 pad H2: Net-(U3-PadA1) -> +1V5
- U3 pad H9: Net-(U3-PadA1) -> +1V5
- U3 pad K2: Net-(U3-PadB2) -> +1V5
- U3 pad K8: Net-(U3-PadB2) -> +1V5
- U3 pad M8: Net-(U3-PadM8) -> VTTREF
- U3 pad N1: Net-(U3-PadB2) -> +1V5
- U3 pad N9: Net-(U3-PadB2) -> +1V5
- U3 pad R1: Net-(U3-PadB2) -> +1V5
- U3 pad R9: Net-(U3-PadB2) -> +1V5
- U4 pad A1: Net-(U4-PadA1) -> +1V5
- U4 pad A8: Net-(U4-PadA1) -> +1V5
- U4 pad B2: Net-(U4-PadB2) -> +1V5
- U4 pad C1: Net-(U4-PadA1) -> +1V5
- U4 pad C9: Net-(U4-PadA1) -> +1V5
- U4 pad D2: Net-(U4-PadA1) -> +1V5
- U4 pad D9: Net-(U4-PadB2) -> +1V5
- U4 pad E9: Net-(U4-PadA1) -> +1V5
- U4 pad F1: Net-(U4-PadA1) -> +1V5
- U4 pad G7: Net-(U4-PadB2) -> +1V5
- U4 pad H1: Net-(U4-PadH1) -> VTTREF
- U4 pad H2: Net-(U4-PadA1) -> +1V5
- U4 pad H9: Net-(U4-PadA1) -> +1V5
- U4 pad K2: Net-(U4-PadB2) -> +1V5
- U4 pad K8: Net-(U4-PadB2) -> +1V5
- U4 pad M8: Net-(U4-PadM8) -> VTTREF
- U4 pad N1: Net-(U4-PadB2) -> +1V5
- U4 pad N9: Net-(U4-PadB2) -> +1V5
- U4 pad R1: Net-(U4-PadB2) -> +1V5
- U4 pad R9: Net-(U4-PadB2) -> +1V5
- U5 pad 2: Net-(U5-Pad2) -> +1V5
- U5 pad 5: Net-(U5-Pad5) -> Vtt
- U5 pad 6: Net-(U5-Pad6) -> VTTREF
- U6 pad 14: Net-(U6-Pad14) -> +1V2
- U6 pad 15: Net-(U6-Pad15) -> ETH0_LED_RX
- U6 pad 16: Net-(U6-Pad16) -> +3V3
- U6 pad 17: Net-(U6-Pad17) -> ETH0_LED_LINK1
- U6 pad 18: Net-(U6-Pad18) -> +1V2
- U6 pad 23: Net-(U6-Pad23) -> +1V2
- U6 pad 26: Net-(U6-Pad26) -> +1V2
- U6 pad 29: Net-(U6-Pad29) -> GND
- U6 pad 30: Net-(U6-Pad30) -> +1V2
- U6 pad 33: Net-(U6-Pad33) -> ETH_RX_DV
- U6 pad 34: Net-(U6-Pad34) -> +3V3
- U6 pad 35: Net-(U6-Pad35) -> ETH_RX_CLK
- U6 pad 36: Net-(U6-Pad36) -> ETH_MDC
- U6 pad 37: Net-(U6-Pad37) -> ETH_MDIO
- U6 pad 38: Net-(U6-Pad38) -> ETH_INT_N
- U6 pad 39: Net-(U6-Pad39) -> +1V2
- U6 pad 40: Net-(U6-Pad40) -> +3V3
- U6 pad 41: Net-(U6-Pad41) -> ETH_REF_CLK
- U6 pad 49: Net-(U6-Pad49) -> GND
- U7 pad A10: Net-(U7-PadA10) -> +1V1
- U7 pad A13: Net-(U7-PadA13) -> +1V1
- U7 pad A2: Net-(U7-PadA2) -> TUSB_RX_D6
- U7 pad A3: Net-(U7-PadA3) -> TUSB_RX_D7
- U7 pad A4: Net-(U7-PadA4) -> TUSB_RX_D9
- U7 pad A5: Net-(U7-PadA5) -> +1V1
- U7 pad A6: Net-(U7-PadA6) -> TUSB_PCLK
- U7 pad A7: Net-(U7-PadA7) -> TUSB_RX_K0
- U7 pad A8: Net-(U7-PadA8) -> TUSB_RX_D13
- U7 pad A9: Net-(U7-PadA9) -> TUSB_RX_D14
- U7 pad B1: Net-(U7-PadB1) -> TUSB_RX_D5
- U7 pad B10: Net-(U7-PadB10) -> +1V1
- U7 pad B11: Net-(U7-PadB11) -> GND
- U7 pad B12: Net-(U7-PadB12) -> TUSB_VSSOSC
- U7 pad B13: Net-(U7-PadB13) -> GND
- U7 pad B14: Net-(U7-PadB14) -> GND
- U7 pad B2: Net-(U7-PadB2) -> +1V8
- U7 pad B3: Net-(U7-PadB3) -> TUSB_RX_D8
- U7 pad B4: Net-(U7-PadB4) -> TUSB_RX_D10
- U7 pad B5: Net-(U7-PadB5) -> TUSB_RX_D11
- U7 pad B6: Net-(U7-PadB6) -> +1V1
- U7 pad B7: Net-(U7-PadB7) -> TUSB_RX_K1
- U7 pad B8: Net-(U7-PadB8) -> TUSB_RX_D12
- U7 pad B9: Net-(U7-PadB9) -> TUSB_RX_D15
- U7 pad C1: Net-(U7-PadC1) -> TUSB_RX_D3
- U7 pad C10: Net-(U7-PadC10) -> +1V1
- U7 pad C11: Net-(U7-PadC11) -> +1V1
- U7 pad C12: Net-(U7-PadC12) -> +1V1
- U7 pad C2: Net-(U7-PadC2) -> TUSB_RX_D4
- U7 pad C3: Net-(U7-PadC3) -> +1V8
- U7 pad C4: Net-(U7-PadC4) -> +1V1
- U7 pad C5: Net-(U7-PadC5) -> TUSB_RX_STAT0
- U7 pad C6: Net-(U7-PadC6) -> TUSB_RX_STAT1
- U7 pad C7: Net-(U7-PadC7) -> TUSB_RX_STAT2
- U7 pad D1: Net-(U7-PadD1) -> TUSB_RX_D2
- U7 pad D12: Net-(U7-PadD12) -> GND
- U7 pad D13: Net-(U7-PadD13) -> +1V1
- U7 pad D14: Net-(U7-PadD14) -> +1V1
- U7 pad D2: Net-(U7-PadD2) -> TUSB_RX_D1
- U7 pad D4: Net-(U7-PadD4) -> +1V8
- U7 pad D7: Net-(U7-PadD7) -> +1V8
- U7 pad D8: Net-(U7-PadD8) -> +1V8
- U7 pad D9: Net-(U7-PadD9) -> +1V8
- U7 pad E1: Net-(U7-PadE1) -> +1V1
- U7 pad E13: Net-(U7-PadE13) -> GND
- U7 pad E2: Net-(U7-PadE2) -> TUSB_RX_D0
- U7 pad E3: Net-(U7-PadE3) -> TUSB_PHY_STATUS
- U7 pad E4: Net-(U7-PadE4) -> +1V8
- U7 pad F1: Net-(U7-PadF1) -> TUSB_RX_VALID
- U7 pad F12: Net-(U7-PadF12) -> GND
- U7 pad F13: Net-(U7-PadF13) -> GND
- U7 pad F2: Net-(U7-PadF2) -> +1V1
- U7 pad F3: Net-(U7-PadF3) -> TUSB_RX_ELECIDLE
- U7 pad F4: Net-(U7-PadF4) -> +1V8
- U7 pad F6: Net-(U7-PadF6) -> GND
- U7 pad F7: Net-(U7-PadF7) -> GND
- U7 pad F8: Net-(U7-PadF8) -> GND
- U7 pad F9: Net-(U7-PadF9) -> GND
- U7 pad G1: Net-(U7-PadG1) -> TUSB_TX_DATAK1
- U7 pad G12: Net-(U7-PadG12) -> GND
- U7 pad G13: Net-(U7-PadG13) -> +1V1
- U7 pad G14: Net-(U7-PadG14) -> +1V1
- U7 pad G2: Net-(U7-PadG2) -> TUSB_TX_D15
- U7 pad G3: Net-(U7-PadG3) -> TUSB_PDOWN1
- U7 pad G4: Net-(U7-PadG4) -> +1V8
- U7 pad G6: Net-(U7-PadG6) -> GND
- U7 pad G7: Net-(U7-PadG7) -> GND
- U7 pad G8: Net-(U7-PadG8) -> GND
- U7 pad G9: Net-(U7-PadG9) -> GND
- U7 pad H1: Net-(U7-PadH1) -> TUSB_TX_D13
- U7 pad H11: Net-(U7-PadH11) -> TUSB_PWRPRESENT
- U7 pad H13: Net-(U7-PadH13) -> GND
- U7 pad H14: USB1_TX_N -> /RAM/USB1TXN
- U7 pad H2: Net-(U7-PadH2) -> TUSB_TX_D14
- U7 pad H3: Net-(U7-PadH3) -> TUSB_PDOWN0
- U7 pad H4: Net-(U7-PadH4) -> +1V8
- U7 pad H6: Net-(U7-PadH6) -> GND
- U7 pad H7: Net-(U7-PadH7) -> GND
- U7 pad H8: Net-(U7-PadH8) -> GND
- U7 pad H9: Net-(U7-PadH9) -> GND
- U7 pad J1: Net-(U7-PadJ1) -> TUSB_TX_DATAK0
- U7 pad J11: Net-(U7-PadJ11) -> TUSB_RESETN
- U7 pad J13: Net-(U7-PadJ13) -> GND
- U7 pad J14: USB1_TX_P -> /RAM/USB1TXP
- U7 pad J2: Net-(U7-PadJ2) -> TUSB_TX_D12
- U7 pad J3: Net-(U7-PadJ3) -> TUSB_PHYRESETN
- U7 pad J6: Net-(U7-PadJ6) -> GND
- U7 pad J7: Net-(U7-PadJ7) -> GND
- U7 pad J8: Net-(U7-PadJ8) -> GND
- U7 pad J9: Net-(U7-PadJ9) -> GND
- U7 pad K1: Net-(U7-PadK1) -> TUSB_TXCLK
- U7 pad K12: Net-(U7-PadK12) -> GND
- U7 pad K13: Net-(U7-PadK13) -> +1V1
- U7 pad K14: Net-(U7-PadK14) -> +1V1
- U7 pad K2: Net-(U7-PadK2) -> +1V1
- U7 pad K3: Net-(U7-PadK3) -> TUSB_TX_ELECIDLE
- U7 pad L1: Net-(U7-PadL1) -> +1V1
- U7 pad L10: Net-(U7-PadL10) -> TUSB_ENAB
- U7 pad L12: Net-(U7-PadL12) -> GND
- U7 pad L2: Net-(U7-PadL2) -> TUSB_TX_D10
- U7 pad L3: Net-(U7-PadL3) -> TUSB_TX_D11
- U7 pad L4: Net-(U7-PadL4) -> +1V8
- U7 pad L5: Net-(U7-PadL5) -> +1V8
- U7 pad L7: Net-(U7-PadL7) -> +1V8
- U7 pad L8: Net-(U7-PadL8) -> +1V8
- U7 pad L9: Net-(U7-PadL9) -> +1V8
- U7 pad M1: Net-(U7-PadM1) -> TUSB_TX_D8
- U7 pad M12: Net-(U7-PadM12) -> GND
- U7 pad M13: Net-(U7-PadM13) -> GND
- U7 pad M2: Net-(U7-PadM2) -> TUSB_TX_D9
- U7 pad M3: Net-(U7-PadM3) -> +1V8
- U7 pad M6: Net-(U7-PadM6) -> TUSB_TX_DETRX_LPBK
- U7 pad M7: Net-(U7-PadM7) -> TUSB_ULPI_DIR
- U7 pad M8: Net-(U7-PadM8) -> TUSB_ULPI_STP
- U7 pad N1: Net-(U7-PadN1) -> TUSB_TX_D7
- U7 pad N10: Net-(U7-PadN10) -> +1V1
- U7 pad N11: Net-(U7-PadN11) -> TUSB_ULPI_NXT
- U7 pad N13: Net-(U7-PadN13) -> GND
- U7 pad N14: Net-(U7-PadN14) -> +1V1
- U7 pad N2: Net-(U7-PadN2) -> TUSB_TX_D5
- U7 pad N3: Net-(U7-PadN3) -> TUSB_TX_D3
- U7 pad N4: Net-(U7-PadN4) -> TUSB_TX_D1
- U7 pad N5: Net-(U7-PadN5) -> +1V1
- U7 pad N6: Net-(U7-PadN6) -> TUSB_ULPI_D7
- U7 pad N7: Net-(U7-PadN7) -> TUSB_ULPI_D5
- U7 pad N8: Net-(U7-PadN8) -> TUSB_ULPI_D3
- U7 pad N9: Net-(U7-PadN9) -> TUSB_ULPI_D0
- U7 pad P1: Net-(U7-PadP1) -> TUSB_TX_D6
- U7 pad P10: Net-(U7-PadP10) -> +1V1
- U7 pad P11: Net-(U7-PadP11) -> TUSB_ULPI_CLK
- U7 pad P12: Net-(U7-PadP12) -> +3V3
- U7 pad P2: Net-(U7-PadP2) -> TUSB_TX_D4
- U7 pad P3: Net-(U7-PadP3) -> TUSB_TX_D2
- U7 pad P4: Net-(U7-PadP4) -> +1V1
- U7 pad P5: Net-(U7-PadP5) -> TUSB_TX_D0
- U7 pad P6: Net-(U7-PadP6) -> TUSB_ULPI_D6
- U7 pad P7: Net-(U7-PadP7) -> TUSB_ULPI_D4
- U7 pad P8: Net-(U7-PadP8) -> TUSB_ULPI_D2
- U7 pad P9: Net-(U7-PadP9) -> TUSB_ULPI_D1
- U8 pad A1: Net-(U8-PadA1) -> GND
- U8 pad A10: Net-(U8-PadA10) -> GND
- U8 pad A2: Net-(U8-PadA2) -> DISP2_RGB17
- U8 pad A3: DISP2_VS -> DISP2_RGB19
- U8 pad A4: DISP2_RGB0 -> DISP2_RGB21
- U8 pad A5: Net-(U8-PadA5) -> DISP2_RGB23
- U8 pad A6: Net-(U8-PadA5) -> Net-(U8-PadA6)
- U8 pad A7: DISP2_RGB3 -> +1V2
- U8 pad B1: Net-(U8-PadB1) -> +1V2
- U8 pad B10: DISP2_RGB6 -> +1V8
- U8 pad B2: Net-(U8-PadB2) -> DISP2_RGB16
- U8 pad B3: DISP2_DE -> DISP2_RGB18
- U8 pad B4: DISP2_HS -> DISP2_RGB20
- U8 pad B5: DISP2_RGB1 -> DISP2_RGB22
- U8 pad B6: DISP2_RGB2 -> Net-(U8-PadB6)
- U8 pad B7: DISP2_RGB4 -> GND
- U8 pad B8: DISP2_RGB7 -> I2C1_SDA
- U8 pad B9: DISP2_RGB5 -> DSI_RST_N
- U8 pad C1: Net-(U8-PadC1) -> DISP2_RGB15
- U8 pad C10: DISP2_RGB8 -> DSI_D3_N
- U8 pad C2: Net-(U8-PadC2) -> DISP2_RGB14
- U8 pad C9: DISP2_RGB9 -> DSI_D3_P
- U8 pad D1: Net-(U8-PadD1) -> DISP2_RGB13
- U8 pad D10: DISP2_RGB14 -> DSI_D2_N
- U8 pad D2: Net-(U8-PadD2) -> DISP2_RGB12
- U8 pad D4: Net-(U8-PadD4) -> GND
- U8 pad D5: Net-(U8-PadD5) -> GND
- U8 pad D6: Net-(U8-PadD6) -> GND
- U8 pad D7: Net-(U8-PadD7) -> GND
- U8 pad D9: DISP2_RGB13 -> DSI_D2_P
- U8 pad E1: Net-(U8-PadE1) -> DISP2_RGB11
- U8 pad E10: DISP2_RGB15 -> +1V2
- U8 pad E2: Net-(U8-PadE2) -> DISP2_RGB10
- U8 pad E4: Net-(U8-PadE4) -> GND
- U8 pad E5: Net-(U8-PadE5) -> GND
- U8 pad E6: Net-(U8-PadE6) -> GND
- U8 pad E7: DISP2_RGB10 -> GND
- U8 pad E9: DISP2_RGB16 -> GND
- U8 pad F1: Net-(U8-PadF1) -> DISP2_RGB9
- U8 pad F10: DISP2_RGB18 -> DSI_CLK_N
- U8 pad F2: Net-(U8-PadF2) -> DISP2_RGB8
- U8 pad F4: Net-(U8-PadE4) -> GND
- U8 pad F5: Net-(U8-PadE4) -> GND
- U8 pad F6: Net-(U8-PadF6) -> GND
- U8 pad F7: DISP2_RGB11 -> GND
- U8 pad F9: DISP2_RGB17 -> DSI_CLK_P
- U8 pad G1: Net-(U8-PadG1) -> DISP2_RGB7
- U8 pad G10: DISP2_PCLK -> DSI_D1_N
- U8 pad G2: Net-(U8-PadG2) -> DISP2_RGB6
- U8 pad G4: Net-(U8-PadG4) -> GND
- U8 pad G5: Net-(U8-PadG4) -> GND
- U8 pad G6: Net-(U8-PadG4) -> GND
- U8 pad G7: DISP2_RGB12 -> GND
- U8 pad G9: DISP2_RGB19 -> DSI_D1_P
- U8 pad H1: Net-(U8-PadH1) -> +1V8
- U8 pad H10: DISP2_RGB21 -> +1V2
- U8 pad H2: Net-(U8-PadH2) -> GND
- U8 pad H9: DISP2_RGB20 -> GND
- U8 pad J1: Net-(U8-PadJ1) -> DISP2_RGB4
- U8 pad J10: DISP2_RGB23 -> DSI_D0_N
- U8 pad J2: Net-(U8-PadJ2) -> DISP2_RGB2
- U8 pad J3: DPLN0+ -> DISP2_RGB0
- U8 pad J4: Net-(U8-PadJ4) -> GND
- U8 pad J5: Net-(U8-PadJ5) -> GND
- U8 pad J6: DPLP1+ -> DISP2_PCLK
- U8 pad J7: Net-(U8-PadJ7) -> DISP2_DE
- U8 pad J8: DPAUX+ -> Net-(R53-Pad1)
- U8 pad J9: Net-(U8-PadJ9) -> DSI_D0_P
- U8 pad K1: Net-(U8-PadK1) -> DISP2_RGB5
- U8 pad K10: DISP2_RGB22 -> GND
- U8 pad K2: Net-(U8-PadK2) -> DISP2_RGB3
- U8 pad K3: DPLN0- -> DISP2_RGB1
- U8 pad K4: Net-(U8-PadJ4) -> +1V2
- U8 pad K5: Net-(U8-PadK5) -> +1V8
- U8 pad K7: Net-(U8-PadK2) -> DISP2_VS
- U8 pad K8: DPAUX- -> DISP2_HS
- U8 pad K9: Net-(U8-PadK9) -> +1V8
- U9 pad 12: Net-(U9-Pad12) -> +1V2
- U9 pad 22: Net-(U9-Pad22) -> DISP1_CLK
- U9 pad 26: Net-(U9-Pad26) -> +1V2
- U9 pad 42: Net-(U9-Pad42) -> +1V2
- U9 pad 47: Net-(U9-Pad47) -> +1V2
- U9 pad 5: Net-(U9-Pad5) -> +1V2
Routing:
- net RAM_D4: track 0.71 -> 62.1 mm, vias 1 -> 4
- net RAM_D6: track 0.71 -> 58.8 mm, vias 1 -> 4
- net RAM_DM1: track 0.71 -> 55.7 mm, vias 1 -> 5
- net RAM_D2: track 0.71 -> 53.8 mm, vias 1 -> 4
- net RAM_D0: track 0.71 -> 52.1 mm, vias 1 -> 4
- net RAM_RESET#: track 1.27 -> 52.1 mm
- net RAM_A15: track 18.5 -> 68.3 mm, vias 2 -> 4
- net RAM_D7: track 0.71 -> 48.2 mm, vias 1 -> 4
- net RAM_D11: track 0.71 -> 46.9 mm, vias 1 -> 4
- net RAM_D5: track 0.71 -> 46.8 mm, vias 1 -> 4
- net RAM_A12: track 19.2 -> 63.9 mm, vias 3 -> 4
- net RAM_D1: track 0.71 -> 45.2 mm, vias 1 -> 4
- net +1V5: track 8.49 -> 52.3 mm, vias 12 -> 41
- net RAM_D9: track 0.71 -> 44.1 mm, vias 1 -> 4
- net RAM_RAS#: track 1.27 -> 44.7 mm, vias 2 -> 3
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- added copper zone on GND1.Cu, net GND
- removed copper zone on GND.Cu, net GND
